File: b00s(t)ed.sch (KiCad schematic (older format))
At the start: 11 parts, among them Q1 IRF7739L1, Q2 2N7002W, U1 LM74610-Q1, U2 NSI50010YT1G

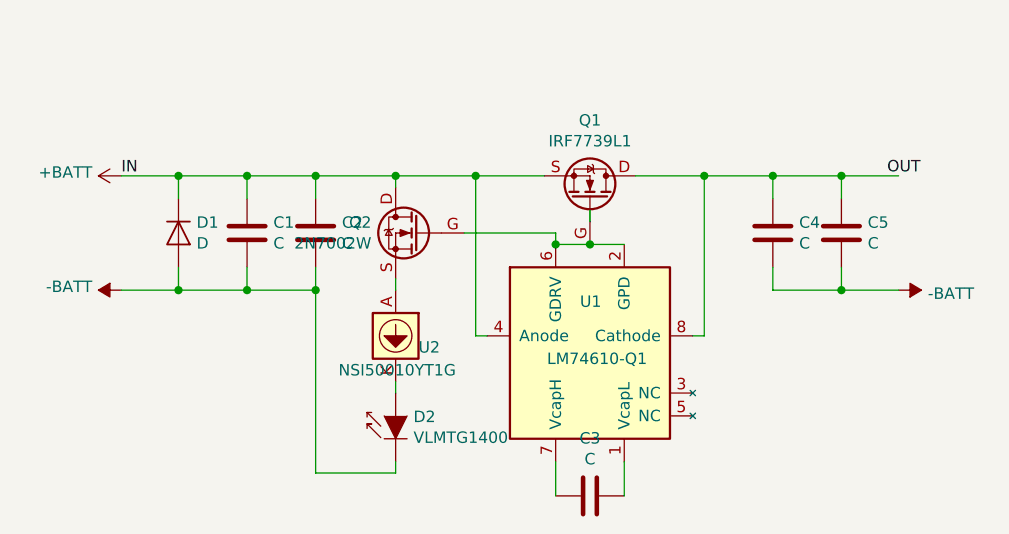
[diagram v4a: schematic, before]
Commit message: Switch over to LM5050-2
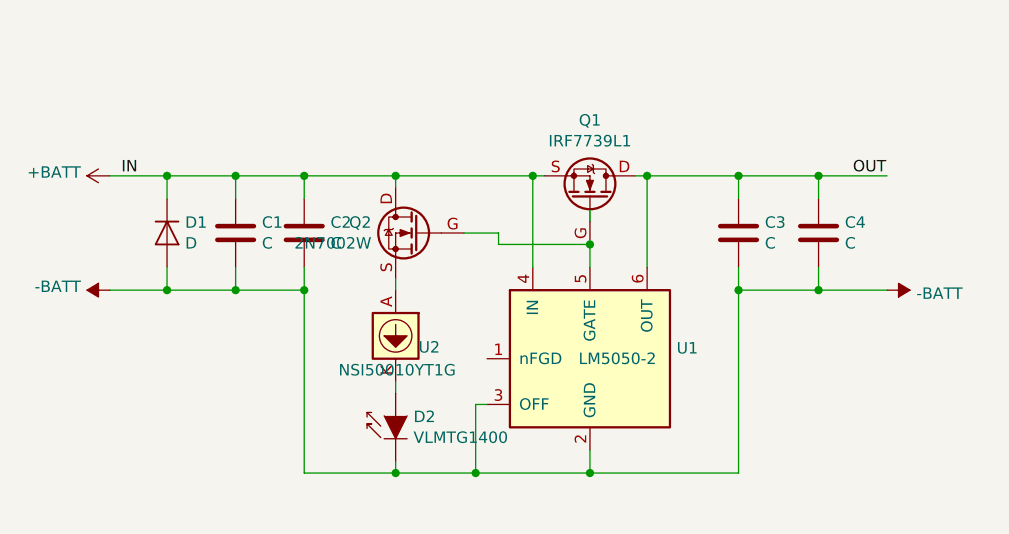
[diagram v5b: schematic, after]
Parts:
- removed C3: C, Capacitor_SMD:C_1206_3216Metric, symbol Device:C
- removed U1: LM74610-Q1, Package_SO:S-PDSO-G8, symbol Power_Management:LM74610-Q1
- added U1: LM5050-2, Package_TO_SOT_SMD:SOT-23-6, symbol Power_Management:LM5050-2
- renumbered C4 to C3, C5 to C4
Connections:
- wire segments 42 -> 45
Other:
- moved on the sheet: C1, C2, C3, C4, D1
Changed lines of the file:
@@
 $EndDescr
-Wire Wire Line
-	5700 2400 5400 2400
 Wire Wire Line
 	5900 2600 5900 2550
@@
 	0    1    -1   0
 $EndComp
-Wire Wire Line
-	6100 2400 6400 2400
 Text Label 3850 2400 0    50   ~ 0
 IN
-Text Label 7200 2400 0    50   ~ 0
+Text Label 7050 2400 0    50   ~ 0
 OUT
-$Comp
-L Power_Management:LM74610-Q1 U1
-U 1 1 5C5374D8
-P 5900 2950
-F 0 "U1" H 5950 2950 50  0000 R CNN
-F 1 "LM74610-Q1" H 6150 2700 50  0000 R CNN
-F 2 "Package_SO:S-PDSO-G8" H 5900 2250 50  0001 C CIN
-F 3 "" H 5900 3150 50  0001 C CNN
-	1    5900 2950
-	1    0    0    -1
-$EndComp
-Wire Wire Line
-	5450 3100 5400 3100
-Wire Wire Line
-	5400 3100 5400 2400
-Wire Wire Line
-	5400 2400 5050 2400
-Wire Wire Line
-	6350 3100 6400 3100
-Wire Wire Line
-	6400 3100 6400 2400
-Connection ~ 6400 2400
-Wire Wire Line
-	6400 2400 6700 2400
-Wire Wire Line
-	5750 2700 5900 2700
-Wire Wire Line
-	6050 2700 5900 2700
-Connection ~ 5900 2700
-$Comp
-L Device:C C3
-U 1 1 5C53C78F
-P 5900 3800
-F 0 "C3" V 5648 3800 50  0000 C CNN
-F 1 "C" V 5739 3800 50  0000 C CNN
-F 2 "Capacitor_SMD:C_1206_3216Metric" H 5938 3650 50  0001 C CNN
-F 3 "" H 5900 3800 50  0001 C CNN
-	1    5900 3800
-	0    1    1    0
-$EndComp
-Wire Wire Line
-	6050 3650 6050 3800
-Wire Wire Line
-	5750 3650 5750 3800
+Wire Wire Line
+	5500 2700 5900 2700
 $Comp
 L Device:D D1
 U 1 1 5C53D25D
-P 4100 2650
-F 0 "D1" V 4054 2729 50  0000 L CNN
-F 1 "D" V 4145 2729 50  0000 L CNN
-F 2 "Diode_SMD:D_SMB" H 4100 2650 50  0001 C CNN
-F 3 "" H 4100 2650 50  0001 C CNN
-	1    4100 2650
+P 4050 2650
+F 0 "D1" V 4004 2729 50  0000 L CNN
+F 1 "D" V 4095 2729 50  0000 L CNN
+F 2 "Diode_SMD:D_SMB" H 4050 2650 50  0001 C CNN
+F 3 "" H 4050 2650 50  0001 C CNN
+	1    4050 2650
 	0    1    1    0
 $EndComp
@@
 L Device:C C2
 U 1 1 5C53D3D8
-P 4700 2650
-F 0 "C2" H 4815 2696 50  0000 L CNN
-F 1 "C" H 4815 2605 50  0000 L CNN
-F 2 "Capacitor_SMD:C_1206_3216Metric" H 4738 2500 50  0001 C CNN
-F 3 "" H 4700 2650 50  0001 C CNN
-	1    4700 2650
-	1    0    0    -1
-$EndComp
-Wire Wire Line
-	4700 2500 4700 2400
-Connection ~ 4700 2400
-Wire Wire Line
-	4700 2400 4400 2400
-Wire Wire Line
-	4400 2500 4400 2400
-Connection ~ 4400 2400
-Wire Wire Line
-	4400 2400 4100 2400
-$Comp
-L Device:C C4
+P 4650 2650
+F 0 "C2" H 4765 2696 50  0000 L CNN
+F 1 "C" H 4765 2605 50  0000 L CNN
+F 2 "Capacitor_SMD:C_1206_3216Metric" H 4688 2500 50  0001 C CNN
+F 3 "" H 4650 2650 50  0001 C CNN
+	1    4650 2650
+	1    0    0    -1
+$EndComp
+Wire Wire Line
+	4650 2500 4650 2400
+Connection ~ 4650 2400
+Wire Wire Line
+	4650 2400 4350 2400
+Wire Wire Line
+	4350 2500 4350 2400
+Connection ~ 4350 2400
+Wire Wire Line
+	4350 2400 4050 2400
+$Comp
+L Device:C C3
 U 1 1 5C53E8AA
-P 6700 2650
-F 0 "C4" H 6815 2696 50  0000 L CNN
-F 1 "C" H 6815 2605 50  0000 L CNN
-F 2 "Capacitor_SMD:C_1206_3216Metric" H 6738 2500 50  0001 C CNN
-F 3 "" H 6700 2650 50  0001 C CNN
-	1    6700 2650
-	1    0    0    -1
-$EndComp
-Wire Wire Line
-	6700 2900 6700 2800
-Wire Wire Line
-	6700 2500 6700 2400
-Connection ~ 6700 2400
-Wire Wire Line
-	6700 2400 7000 2400
+P 6550 2650
+F 0 "C3" H 6665 2696 50  0000 L CNN
+F 1 "C" H 6665 2605 50  0000 L CNN
+F 2 "Capacitor_SMD:C_1206_3216Metric" H 6588 2500 50  0001 C CNN
+F 3 "" H 6550 2650 50  0001 C CNN
+	1    6550 2650
+	1    0    0    -1
+$EndComp
+Wire Wire Line
+	6550 2900 6550 2800
+Wire Wire Line
+	6550 2500 6550 2400
+Connection ~ 6550 2400
+Wire Wire Line
+	6550 2400 6900 2400
 $Comp
 L Device:C C1
 U 1 1 5C54035D
-P 4400 2650
-F 0 "C1" H 4515 2696 50  0000 L CNN
-F 1 "C" H 4515 2605 50  0000 L CNN
-F 2 "Capacitor_SMD:C_1206_3216Metric" H 4438 2500 50  0001 C CNN
-F 3 "" H 4400 2650 50  0001 C CNN
-	1    4400 2650
-	1    0    0    -1
-$EndComp
-Wire Wire Line
-	4100 2500 4100 2400
-Connection ~ 4100 2400
-Wire Wire Line
-	4100 2400 3850 2400
-$Comp
-L power:+BATT #PWR0101
+P 4350 2650
+F 0 "C1" H 4465 2696 50  0000 L CNN
+F 1 "C" H 4465 2605 50  0000 L CNN
+F 2 "Capacitor_SMD:C_1206_3216Metric" H 4388 2500 50  0001 C CNN
+F 3 "" H 4350 2650 50  0001 C CNN
+	1    4350 2650
+	1    0    0    -1
+$EndComp
+Wire Wire Line
+	4050 2500 4050 2400
+Connection ~ 4050 2400
+Wire Wire Line
+	4050 2400 3800 2400
+$Comp
+L power:+BATT #PWR01
 U 1 1 5C5419B9
-P 3850 2400
-F 0 "#PWR0101" H 3850 2250 50  0001 C CNN
-F 1 "+BATT" V 3865 2527 50  0000 L CNN
-F 2 "" H 3850 2400 50  0001 C CNN
-F 3 "" H 3850 2400 50  0001 C CNN
-	1    3850 2400
+P 3800 2400
+F 0 "#PWR01" H 3800 2250 50  0001 C CNN
+F 1 "+BATT" V 3815 2527 50  0000 L CNN
+F 2 "" H 3800 2400 50  0001 C CNN
+F 3 "" H 3800 2400 50  0001 C CNN
+	1    3800 2400
 	0    -1   -1   0
 $EndComp
 $Comp
-L power:-BATT #PWR0103
+L power:-BATT #PWR02
 U 1 1 5C54344F
-P 3850 2900
-F 0 "#PWR0103" H 3850 2750 50  0001 C CNN
-F 1 "-BATT" V 3865 3027 50  0000 L CNN
-F 2 "" H 3850 2900 50  0001 C CNN
-F 3 "" H 3850 2900 50  0001 C CNN
-	1    3850 2900
+P 3800 2900
+F 0 "#PWR02" H 3800 2750 50  0001 C CNN
+F 1 "-BATT" V 3815 3027 50  0000 L CNN
+F 2 "" H 3800 2900 50  0001 C CNN
+F 3 "" H 3800 2900 50  0001 C CNN
+	1    3800 2900
 	0    -1   -1   0
 $EndComp
 $Comp
-L power:-BATT #PWR0104
+L power:-BATT #PWR03
 U 1 1 5C544FA1
-P 7250 2900
-F 0 "#PWR0104" H 7250 2750 50  0001 C CNN
-F 1 "-BATT" V 7265 3028 50  0000 L CNN
-F 2 "" H 7250 2900 50  0001 C CNN
-F 3 "" H 7250 2900 50  0001 C CNN
-	1    7250 2900
+P 7200 2900
+F 0 "#PWR03" H 7200 2750 50  0001 C CNN
+F 1 "-BATT" V 7215 3028 50  0000 L CNN
+F 2 "" H 7200 2900 50  0001 C CNN
+F 3 "" H 7200 2900 50  0001 C CNN
+	1    7200 2900
 	0    1    1    0
 $EndComp
 Wire Wire Line
-	6700 2900 7000 2900
-Wire Wire Line
-	3850 2900 4100 2900
-Wire Wire Line
-	4700 2900 4700 2800
-Wire Wire Line
-	4400 2800 4400 2900
-Connection ~ 4400 2900
-Wire Wire Line
-	4400 2900 4700 2900
-Wire Wire Line
-	4100 2800 4100 2900
-Connection ~ 4100 2900
-Wire Wire Line
-	4100 2900 4400 2900
-$Comp
-L Device:C C5
+	6550 2900 6900 2900
+Wire Wire Line
+	3800 2900 4050 2900
+Wire Wire Line
+	4650 2900 4650 2800
+Wire Wire Line
+	4350 2800 4350 2900
+Connection ~ 4350 2900
+Wire Wire Line
+	4350 2900 4650 2900
+Wire Wire Line
+	4050 2800 4050 2900
+Connection ~ 4050 2900
+Wire Wire Line
+	4050 2900 4350 2900
+$Comp
+L Device:C C4
 U 1 1 5C555923
-P 7000 2650
-F 0 "C5" H 7115 2696 50  0000 L CNN
-F 1 "C" H 7115 2605 50  0000 L CNN
-F 2 "Capacitor_SMD:C_1206_3216Metric" H 7038 2500 50  0001 C CNN
-F 3 "" H 7000 2650 50  0001 C CNN
-	1    7000 2650
-	1    0    0    -1
-$EndComp
-Wire Wire Line
-	7000 2500 7000 2400
-Connection ~ 7000 2400
-Wire Wire Line
-	7000 2400 7250 2400
-Wire Wire Line
-	7000 2800 7000 2900
-Connection ~ 7000 2900
-Wire Wire Line
-	7000 2900 7250 2900
+P 6900 2650
+F 0 "C4" H 7015 2696 50  0000 L CNN
+F 1 "C" H 7015 2605 50  0000 L CNN
+F 2 "Capacitor_SMD:C_1206_3216Metric" H 6938 2500 50  0001 C CNN
+F 3 "" H 6900 2650 50  0001 C CNN
+	1    6900 2650
+	1    0    0    -1
+$EndComp
+Wire Wire Line
+	6900 2500 6900 2400
+Connection ~ 6900 2400
+Wire Wire Line
+	6900 2400 7200 2400
+Wire Wire Line
+	6900 2800 6900 2900
+Connection ~ 6900 2900
+Wire Wire Line
+	6900 2900 7200 2900
 $Comp
 L Regulator_Current:NSI50010YT1G U2
@@
 	0    -1   -1   0
 $EndComp
-Connection ~ 5400 2400
 Wire Wire Line
 	5050 2400 5050 2450
 Wire Wire Line
-	5050 2400 4700 2400
+	5050 2400 4650 2400
 Wire Wire Line
 	5050 2850 5050 2900
@@
 	5050 3650 5050 3700
 Wire Wire Line
-	5050 3700 4700 3700
-Wire Wire Line
-	4700 3700 4700 2900
-Connection ~ 4700 2900
+	5050 3700 4650 3700
+Wire Wire Line
+	4650 3700 4650 2900
+Connection ~ 4650 2900
 Connection ~ 5050 2400
 Wire Wire Line
-	5750 2700 5750 2650
-Wire Wire Line
-	5750 2650 5350 2650
-Connection ~ 5750 2700
+	5500 2700 5500 2650
+Wire Wire Line
+	5500 2650 5350 2650
 $Comp
 L Transistor_FET:2N7002W Q2
@@
 	-1   0    0    -1
 $EndComp
+$Comp
+L Power_Management:LM5050-2 U1
+U 1 1 5C62AAD7
+P 5900 3200
+F 0 "U1" H 6279 3246 50  0000 L CNN
+F 1 "LM5050-2" H 5850 3200 50  0000 L CNN
+F 2 "Package_TO_SOT_SMD:SOT-23-6" H 5900 2800 50  0001 C CIN
+F 3 "http://www.ti.com/lit/ds/symlink/lm74610-q1.pdf" H 5900 3400 50  0001 C CNN
+	1    5900 3200
+	1    0    0    -1
+$EndComp
+Wire Wire Line
+	5050 2400 5650 2400
+Wire Wire Line
+	6100 2400 6150 2400
+Wire Wire Line
+	5650 2800 5650 2400
+Connection ~ 5650 2400
+Wire Wire Line
+	5650 2400 5700 2400
+Wire Wire Line
+	6150 2800 6150 2400
+Connection ~ 6150 2400
+Wire Wire Line
+	6150 2400 6550 2400
+Wire Wire Line
+	5900 2800 5900 2700
+Connection ~ 5900 2700
+Wire Wire Line
+	5050 3700 5400 3700
+Wire Wire Line
+	5900 3700 5900 3600
+Connection ~ 5050 3700
+Wire Wire Line
+	5900 3700 6550 3700
+Wire Wire Line
+	6550 3700 6550 2900
+Connection ~ 5900 3700
+Connection ~ 6550 2900
+Wire Wire Line
+	5450 3400 5400 3400
+Wire Wire Line
+	5400 3400 5400 3700
+Connection ~ 5400 3700
+Wire Wire Line
+	5400 3700 5900 3700
 $EndSCHEMATC

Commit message: Switch over to LM5050-1
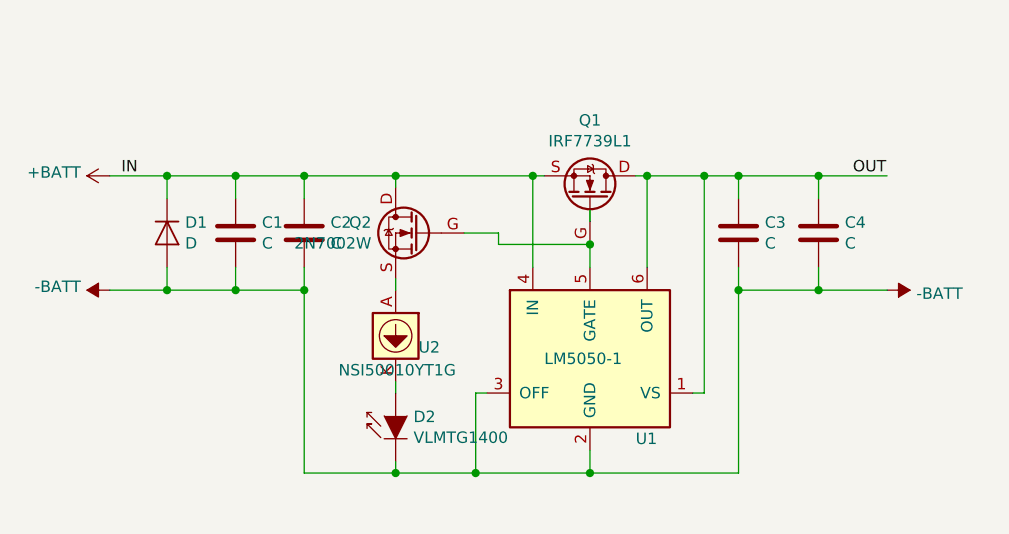
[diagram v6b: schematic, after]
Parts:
- removed U1: LM5050-2, Package_TO_SOT_SMD:SOT-23-6, symbol Power_Management:LM5050-2
- added U1: LM5050-1, Package_TO_SOT_SMD:SOT-23-6, symbol Power_Management:LM5050-1
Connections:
- wire segments 45 -> 48
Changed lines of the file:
@@
 	-1   0    0    -1
-$EndComp
-$Comp
-L Power_Management:LM5050-2 U1
-U 1 1 5C62AAD7
-P 5900 3200
-F 0 "U1" H 6279 3246 50  0000 L CNN
-F 1 "LM5050-2" H 5850 3200 50  0000 L CNN
-F 2 "Package_TO_SOT_SMD:SOT-23-6" H 5900 2800 50  0001 C CIN
-F 3 "http://www.ti.com/lit/ds/symlink/lm74610-q1.pdf" H 5900 3400 50  0001 C CNN
-	1    5900 3200
-	1    0    0    -1
 $EndComp
 Wire Wire Line
@@
 Connection ~ 6150 2400
 Wire Wire Line
-	6150 2400 6550 2400
+	6150 2400 6400 2400
 Wire Wire Line
 	5900 2800 5900 2700
@@
 Connection ~ 6550 2900
 Wire Wire Line
-	5450 3400 5400 3400
+	5450 3350 5400 3350
 Wire Wire Line
-	5400 3400 5400 3700
+	5400 3350 5400 3700
 Connection ~ 5400 3700
 Wire Wire Line
 	5400 3700 5900 3700
+$Comp
+L Power_Management:LM5050-1 U1
+U 1 1 5C62EAA0
+P 5900 3200
+F 0 "U1" H 6100 2850 50  0000 L CNN
+F 1 "LM5050-1" H 5700 3200 50  0000 L CNN
+F 2 "Package_TO_SOT_SMD:SOT-23-6" H 5900 2800 50  0001 C CIN
+F 3 "http://www.ti.com/lit/ds/symlink/lm74610-q1.pdf" H 5900 3400 50  0001 C CNN
+	1    5900 3200
+	1    0    0    -1
+$EndComp
+Wire Wire Line
+	6350 3350 6400 3350
+Wire Wire Line
+	6400 3350 6400 2400
+Connection ~ 6400 2400
+Wire Wire Line
+	6400 2400 6550 2400
 $EndSCHEMATC

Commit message: Fucking kicad has pin mappings wrong
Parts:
- Q2: footprint Package_TO_SOT_SMD:SOT-323_SC-70 -> Package_TO_SOT_SMD:SOT-323_SC-70-FET
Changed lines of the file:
@@
 F 0 "Q2" H 5356 2696 50  0000 L CNN
 F 1 "2N7002W" H 5356 2605 50  0000 L CNN
-F 2 "Package_TO_SOT_SMD:SOT-323_SC-70" H 5350 2575 50  0001 L CIN
+F 2 "Package_TO_SOT_SMD:SOT-323_SC-70-FET" H 5350 2575 50  0001 L CIN
 F 3 "https://www.onsemi.com/pub/Collateral/2N7002W-D.PDF" H 5350 2725 50  0001 L CNN
 	1    5150 2650
